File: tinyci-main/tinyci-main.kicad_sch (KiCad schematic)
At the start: 47 parts, among them J1 Jack-DC, J2 Jack-DC, J3 Jack-DC, J4 Conn_01x13_Male, J5 Conn_01x13_Male, J6 Jack-DC, J7 Jack-DC, J8 Conn_01x06_Male, J9 Conn_01x06_Male, K1 SANYOU_SRD_Form_C, K2 SANYOU_SRD_Form_C, K3 SANYOU_SRD_Form_C, K4 SANYOU_SRD_Form_C, Q1 BC337, Q2 BC337, Q3 BC337, Q4 BC337, U1 AMS1117-3.3

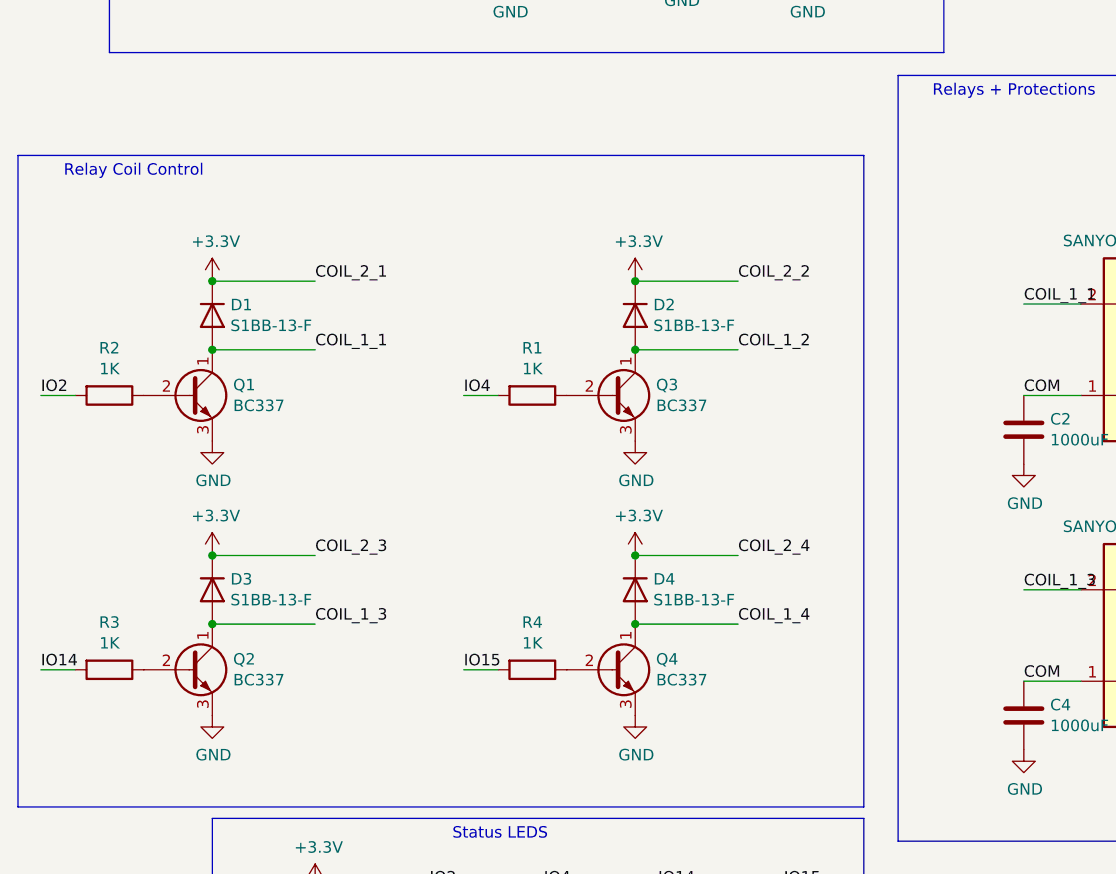
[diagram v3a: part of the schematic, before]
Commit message: tinyci-main: Replaced the relay coil transistors by SMD parts to speed up the board assembly.
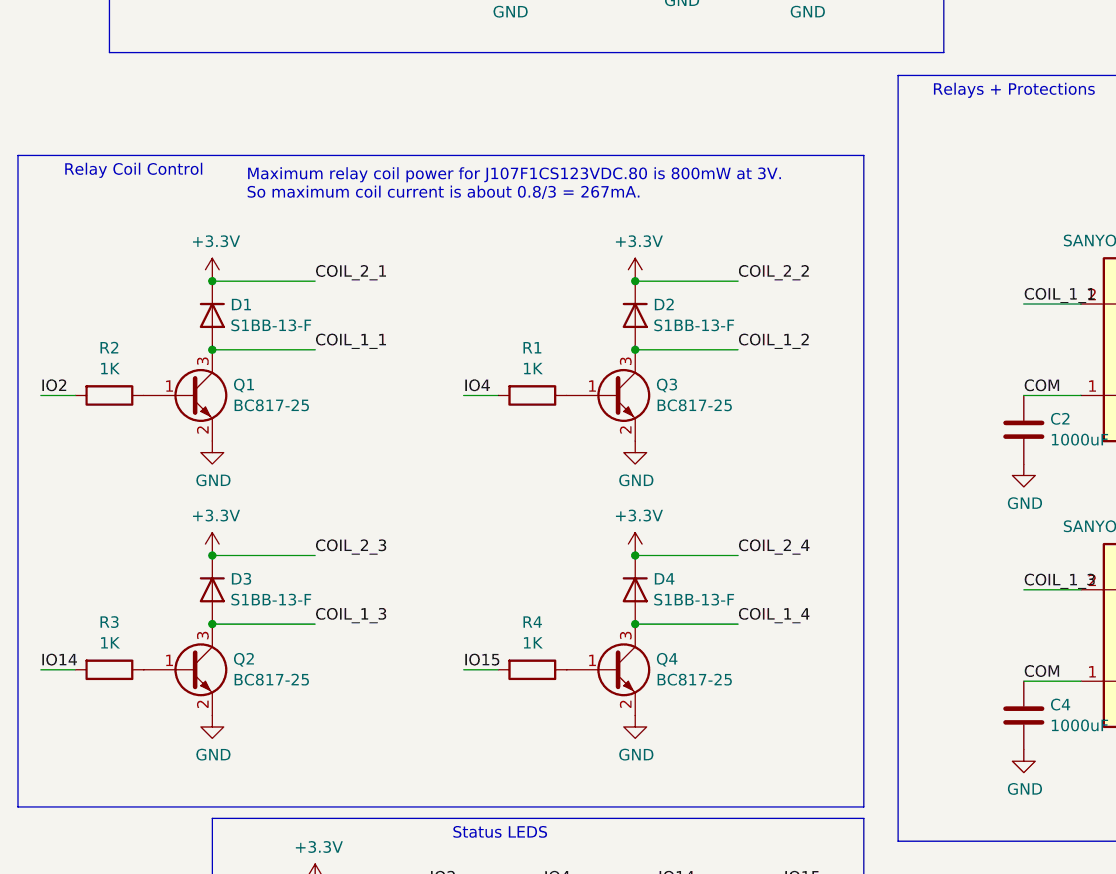
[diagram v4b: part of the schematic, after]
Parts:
- D1, D2, D3, D4: symbol Diode:1N4001 -> Device:D
- Q1, Q2, Q3, Q4: value BC337 -> BC817-25; footprint Package_TO_SOT_THT:TO-92_Inline -> Package_TO_SOT_SMD:SOT-23; symbol Transistor_BJT:BC337 -> Transistor_BJT:BC817
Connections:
- net COIL_1_1: now also Q1.3 (C); no longer Q1.1 (C)
- net COIL_1_2: now also Q3.3 (C); no longer Q3.1 (C)
- net COIL_1_3: now also Q2.3 (C); no longer Q2.1 (C)
- net COIL_1_4: now also Q4.3 (C); no longer Q4.1 (C)
- net GND: now also Q1.2 (E), Q2.2 (E), Q3.2 (E), Q4.2 (E); no longer Q1.3 (E), Q2.3 (E), Q3.3 (E), Q4.3 (E)
- net at R1.1: now also Q3.1 (B); no longer Q3.2 (B)
- net at R2.1: now also Q1.1 (B); no longer Q1.2 (B)
- net at R3.1: now also Q2.1 (B); no longer Q2.2 (B)
- net at R4.1: now also Q4.1 (B); no longer Q4.2 (B)
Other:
- note added: "Maximum relay coil power for J107F1CS123VDC.80 is 800mW at 3V. So maximum coil current is about 0.8/3 = 267mA."
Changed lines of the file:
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@@
+    (effects (font (size 1.27 1.27)) (justify left bottom))
+  )
+  (text "Maximum relay coil power for J107F1CS123VDC.80 is 800mW at 3V.\nSo maximum coil current is about 0.8/3 = 267mA."
+    (at 40.64 92.71 0)
     (effects (font (size 1.27 1.27)) (justify left bottom))
   )
@@
     (pin "1")
   )
-  (symbol (lib_id "Diode:1N4001") (at 83.82 105.41 270) (unit 1)
+  (symbol (lib_id "Device:D") (at 83.82 105.41 270) (unit 1)
     (in_bom yes) (on_board yes)
     (property "Reference" "D2" (id 0) (at 85.8266 104.2416 90)
@@
     (pin "1")
   )
-  (symbol (lib_id "Diode:1N4001") (at 36.83 105.41 270) (unit 1)
+  (symbol (lib_id "Device:D") (at 36.83 105.41 270) (unit 1)
     (in_bom yes) (on_board yes)
     (property "Reference" "D1" (id 0) (at 38.8366 104.2416 90)
@@
     (pin "1")
   )
-  (symbol (lib_id "Diode:1N4001") (at 36.83 135.89 270) (unit 1)
+  (symbol (lib_id "Device:D") (at 36.83 135.89 270) (unit 1)
     (in_bom yes) (on_board yes)
     (property "Reference" "D3" (id 0) (at 38.8366 134.7216 90)
@@
     (pin "1")
   )
-  (symbol (lib_id "Diode:1N4001") (at 83.82 135.89 270) (unit 1)
+  (symbol (lib_id "Device:D") (at 83.82 135.89 270) (unit 1)
     (in_bom yes) (on_board yes)
     (property "Reference" "D4" (id 0) (at 85.8266 134.7216 90)
@@
     (pin "2")
   )
-  (symbol (lib_id "Transistor_BJT:BC337") (at 34.29 114.3 0) (unit 1)
+  (symbol (lib_id "Transistor_BJT:BC817") (at 34.29 114.3 0) (unit 1)
     (in_bom yes) (on_board yes)
     (property "Reference" "Q1" (id 0) (at 39.1414 113.1316 0)
       (effects (font (size 1.27 1.27)) (justify left))
     )
-    (property "Value" "BC337" (id 1) (at 39.1414 115.443 0)
-      (effects (font (size 1.27 1.27)) (justify left))
-    )
-    (property "Footprint" "Package_TO_SOT_THT:TO-92_Inline" (id 2) (at 39.37 116.205 0)
+    (property "Value" "BC817-25" (id 1) (at 39.1414 115.443 0)
+      (effects (font (size 1.27 1.27)) (justify left))
+    )
+    (property "Footprint" "Package_TO_SOT_SMD:SOT-23" (id 2) (at 39.37 116.205 0)
       (effects (font (size 1.27 1.27) italic) (justify left) hide)
     )
-    (property "Datasheet" "http://www.fairchildsemi.com/ds/BC/BC337.pdf" (id 3) (at 34.29 114.3 0)
+    (property "Datasheet" "https://www.onsemi.com/pub/Collateral/BC818-D.pdf" (id 3) (at 34.29 114.3 0)
       (effects (font (size 1.27 1.27)) (justify left) hide)
     )
@@
     (pin "3")
   )
-  (symbol (lib_id "Transistor_BJT:BC337") (at 34.29 144.78 0) (unit 1)
+  (symbol (lib_id "Transistor_BJT:BC817") (at 34.29 144.78 0) (unit 1)
     (in_bom yes) (on_board yes)
     (property "Reference" "Q2" (id 0) (at 39.1414 143.6116 0)
       (effects (font (size 1.27 1.27)) (justify left))
     )
-    (property "Value" "BC337" (id 1) (at 39.1414 145.923 0)
-      (effects (font (size 1.27 1.27)) (justify left))
-    )
-    (property "Footprint" "Package_TO_SOT_THT:TO-92_Inline" (id 2) (at 39.37 146.685 0)
+    (property "Value" "BC817-25" (id 1) (at 39.1414 145.923 0)
+      (effects (font (size 1.27 1.27)) (justify left))
+    )
+    (property "Footprint" "Package_TO_SOT_SMD:SOT-23" (id 2) (at 39.37 146.685 0)
       (effects (font (size 1.27 1.27) italic) (justify left) hide)
     )
-    (property "Datasheet" "http://www.fairchildsemi.com/ds/BC/BC337.pdf" (id 3) (at 34.29 144.78 0)
+    (property "Datasheet" "https://www.onsemi.com/pub/Collateral/BC818-D.pdf" (id 3) (at 34.29 144.78 0)
       (effects (font (size 1.27 1.27)) (justify left) hide)
     )
@@
     (pin "3")
   )
-  (symbol (lib_id "Transistor_BJT:BC337") (at 81.28 144.78 0) (unit 1)
+  (symbol (lib_id "Transistor_BJT:BC817") (at 81.28 144.78 0) (unit 1)
     (in_bom yes) (on_board yes)
     (property "Reference" "Q4" (id 0) (at 86.1314 143.6116 0)
       (effects (font (size 1.27 1.27)) (justify left))
     )
-    (property "Value" "BC337" (id 1) (at 86.1314 145.923 0)
-      (effects (font (size 1.27 1.27)) (justify left))
-    )
-    (property "Footprint" "Package_TO_SOT_THT:TO-92_Inline" (id 2) (at 86.36 146.685 0)
+    (property "Value" "BC817-25" (id 1) (at 86.1314 145.923 0)
+      (effects (font (size 1.27 1.27)) (justify left))
+    )
+    (property "Footprint" "Package_TO_SOT_SMD:SOT-23" (id 2) (at 86.36 146.685 0)
       (effects (font (size 1.27 1.27) italic) (justify left) hide)
     )
-    (property "Datasheet" "http://www.fairchildsemi.com/ds/BC/BC337.pdf" (id 3) (at 81.28 144.78 0)
+    (property "Datasheet" "https://www.onsemi.com/pub/Collateral/BC818-D.pdf" (id 3) (at 81.28 144.78 0)
       (effects (font (size 1.27 1.27)) (justify left) hide)
     )
@@
     (pin "3")
   )
-  (symbol (lib_id "Transistor_BJT:BC337") (at 81.28 114.3 0) (unit 1)
+  (symbol (lib_id "Transistor_BJT:BC817") (at 81.28 114.3 0) (unit 1)
     (in_bom yes) (on_board yes)
     (property "Reference" "Q3" (id 0) (at 86.1314 113.1316 0)
       (effects (font (size 1.27 1.27)) (justify left))
     )
-    (property "Value" "BC337" (id 1) (at 86.1314 115.443 0)
-      (effects (font (size 1.27 1.27)) (justify left))
-    )
-    (property "Footprint" "Package_TO_SOT_THT:TO-92_Inline" (id 2) (at 86.36 116.205 0)
+    (property "Value" "BC817-25" (id 1) (at 86.1314 115.443 0)
+      (effects (font (size 1.27 1.27)) (justify left))
+    )
+    (property "Footprint" "Package_TO_SOT_SMD:SOT-23" (id 2) (at 86.36 116.205 0)
       (effects (font (size 1.27 1.27) italic) (justify left) hide)
     )
-    (property "Datasheet" "http://www.fairchildsemi.com/ds/BC/BC337.pdf" (id 3) (at 81.28 114.3 0)
+    (property "Datasheet" "https://www.onsemi.com/pub/Collateral/BC818-D.pdf" (id 3) (at 81.28 114.3 0)
       (effects (font (size 1.27 1.27)) (justify left) hide)
     )
@@
     )
     (path "/00000000-0000-0000-0000-00005fb27126"
-      (reference "Q1") (unit 1) (value "BC337") (footprint "Package_TO_SOT_THT:TO-92_Inline")
+      (reference "Q1") (unit 1) (value "BC817-25") (footprint "Package_TO_SOT_SMD:SOT-23")
     )
     (path "/00000000-0000-0000-0000-00005fb2a1e1"
-      (reference "Q2") (unit 1) (value "BC337") (footprint "Package_TO_SOT_THT:TO-92_Inline")
+      (reference "Q2") (unit 1) (value "BC817-25") (footprint "Package_TO_SOT_SMD:SOT-23")
     )
     (path "/00000000-0000-0000-0000-00005fb2acc7"
-      (reference "Q3") (unit 1) (value "BC337") (footprint "Package_TO_SOT_THT:TO-92_Inline")
+      (reference "Q3") (unit 1) (value "BC817-25") (footprint "Package_TO_SOT_SMD:SOT-23")
     )
     (path "/00000000-0000-0000-0000-00005fb2a79c"
-      (reference "Q4") (unit 1) (value "BC337") (footprint "Package_TO_SOT_THT:TO-92_Inline")
+      (reference "Q4") (unit 1) (value "BC817-25") (footprint "Package_TO_SOT_SMD:SOT-23")
     )
     (path "/00000000-0000-0000-0000-00005faa913a"
